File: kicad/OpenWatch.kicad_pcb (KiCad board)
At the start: 2 copper layers, 60 parts, among them J1 USB_microB_2040002-1, J3 Conn_02x05_Odd_Even, J4 Vibration Motor, J6 Conn_01x05, U1 STM32F303RCT6-48, U3 TSP70933DBVR, U7 RT9818A-18GV

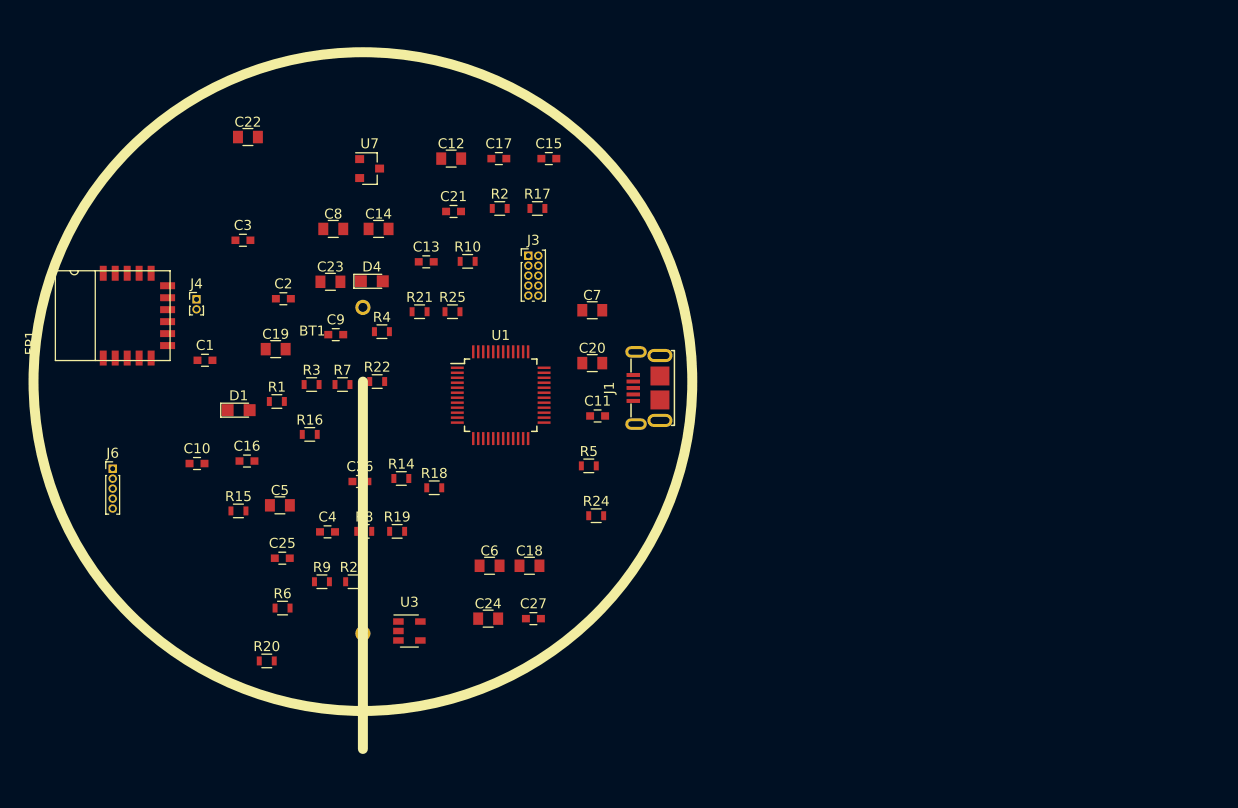
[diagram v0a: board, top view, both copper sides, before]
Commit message: Add all components to be routed to PCB
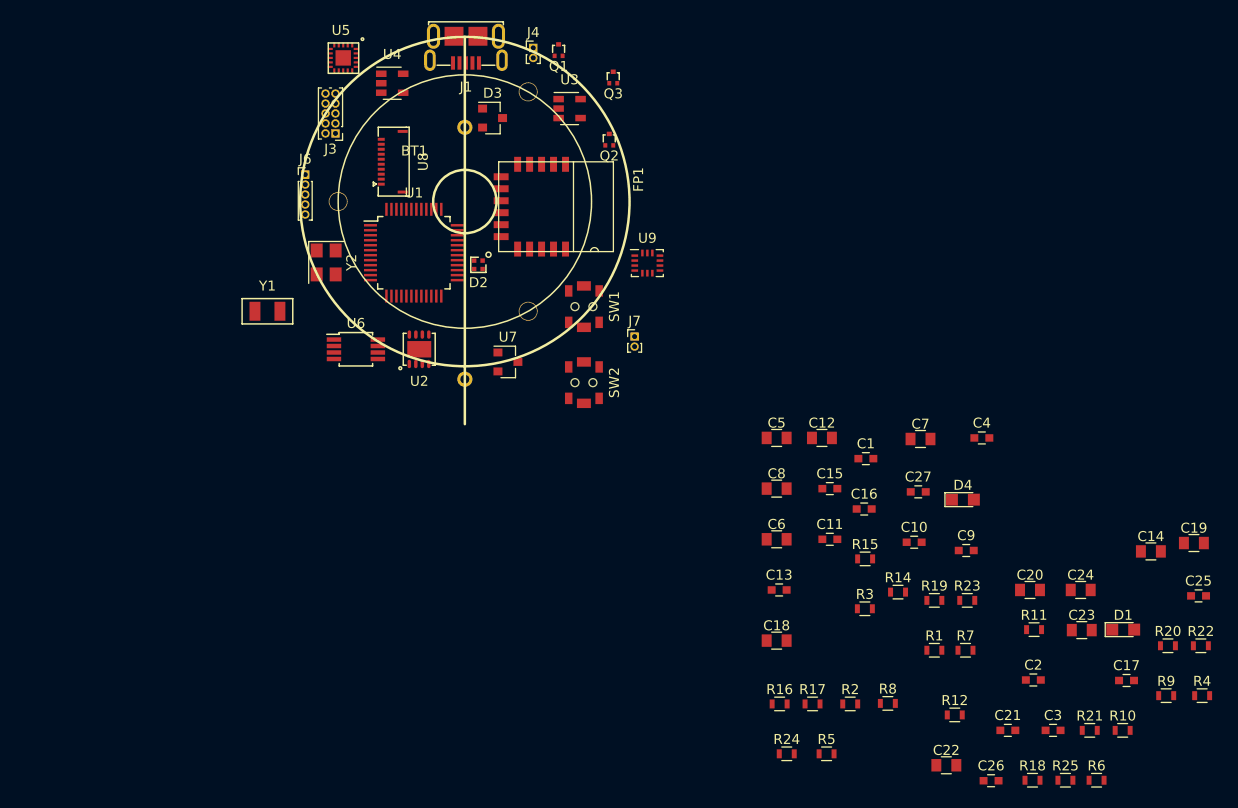
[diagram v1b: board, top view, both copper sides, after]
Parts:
- added D2: LED_ARGB, open_watch:SMLP34RGB2W3, F.Cu at (141.8, 104.6)
- added D3: BAT54, TO_SOT_Packages_SMD:SOT-23, F.Cu at (143.2, 89.8)
- added J7: Conn_01x02, Pin_Headers:Pin_Header_Straight_1x02_Pitch1.00mm, F.Cu at (157.5, 111.8)
- added Q1: RUM002N02T2L, open_watch:VMT3, F.Cu at (149.9, 82.5)
- added Q2: RUM002N02T2L, open_watch:VMT3, F.Cu at (154.9, 91.4)
- added Q3: RUM002N02T2L, open_watch:VMT3, F.Cu at (155.3, 85.2)
- added R11: DNP-0, Resistors_SMD:R_0603, F.Cu at (197.5, 141.1)
- added R12: DNP-0, Resistors_SMD:R_0603, F.Cu at (189.6, 149.7)
- added SW1: SW_Push, open_watch:PTS820_J15M_SMTR_LFS, F.Cu at (152.4, 108.8)
- added SW2: SW_Push, open_watch:PTS820_J15M_SMTR_LFS, F.Cu at (152.4, 116.4)
- added U2: TPS2113ADRBR, open_watch:SON-8, F.Cu at (135.9, 113.0)
- added U4: MCP73831T-2ACI, TO_SOT_Packages_SMD:SOT-23-5, F.Cu at (133.2, 86.4)
- added U5: AT42QT1070-MMHR, open_watch:AT42QT1070-MMHR, F.Cu at (126.8, 82.3)
- added U6: TPS60241DGKR, Housings_SSOP:MSOP-8_3x3mm_Pitch0.65mm, F.Cu at (129.5, 113.0)
- added U8: WM1389CT-ND, open_watch:Molex_FPC_5034801000, F.Cu at (134.9, 94.2)
- added U9: LSM6DSL, Housings_LGA:Bosch_LGA-14_3x2.5mm_Pitch0.5mm, F.Cu at (158.8, 104.4)
- added Y1: ECS.327, open_watch:ECX-31B, F.Cu at (120.7, 109.2)
- added Y2: FA-238, Crystals:Crystal_SMD_SeikoEpson_FA238V-4pin_3.2x2.5mm, F.Cu at (126.6, 104.3)
- moved C3 94.9 mm to (199.4, 151.2)
- moved C22 94.2 mm to (188.7, 154.7)
- moved C19 94.1 mm to (213.6, 132.5)
- moved C25 91.9 mm to (214.0, 137.8)
- moved D1 91.4 mm to (206.5, 141.1)
- moved R20 90.4 mm to (210.9, 142.8)
- moved R4 90.0 mm to (214.4, 147.8)
- moved R22 86.7 mm to (214.2, 142.8)
- moved R9 85.4 mm to (210.8, 147.8)
- moved C2 84.3 mm to (197.5, 146.2)
- moved C14 83.9 mm to (209.2, 133.3)
- moved R6 83.4 mm to (203.8, 156.2)
- moved C23 83.0 mm to (202.3, 141.2)
- moved C17 81.8 mm to (206.8, 146.2)
- moved R10 80.8 mm to (206.4, 151.2)
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
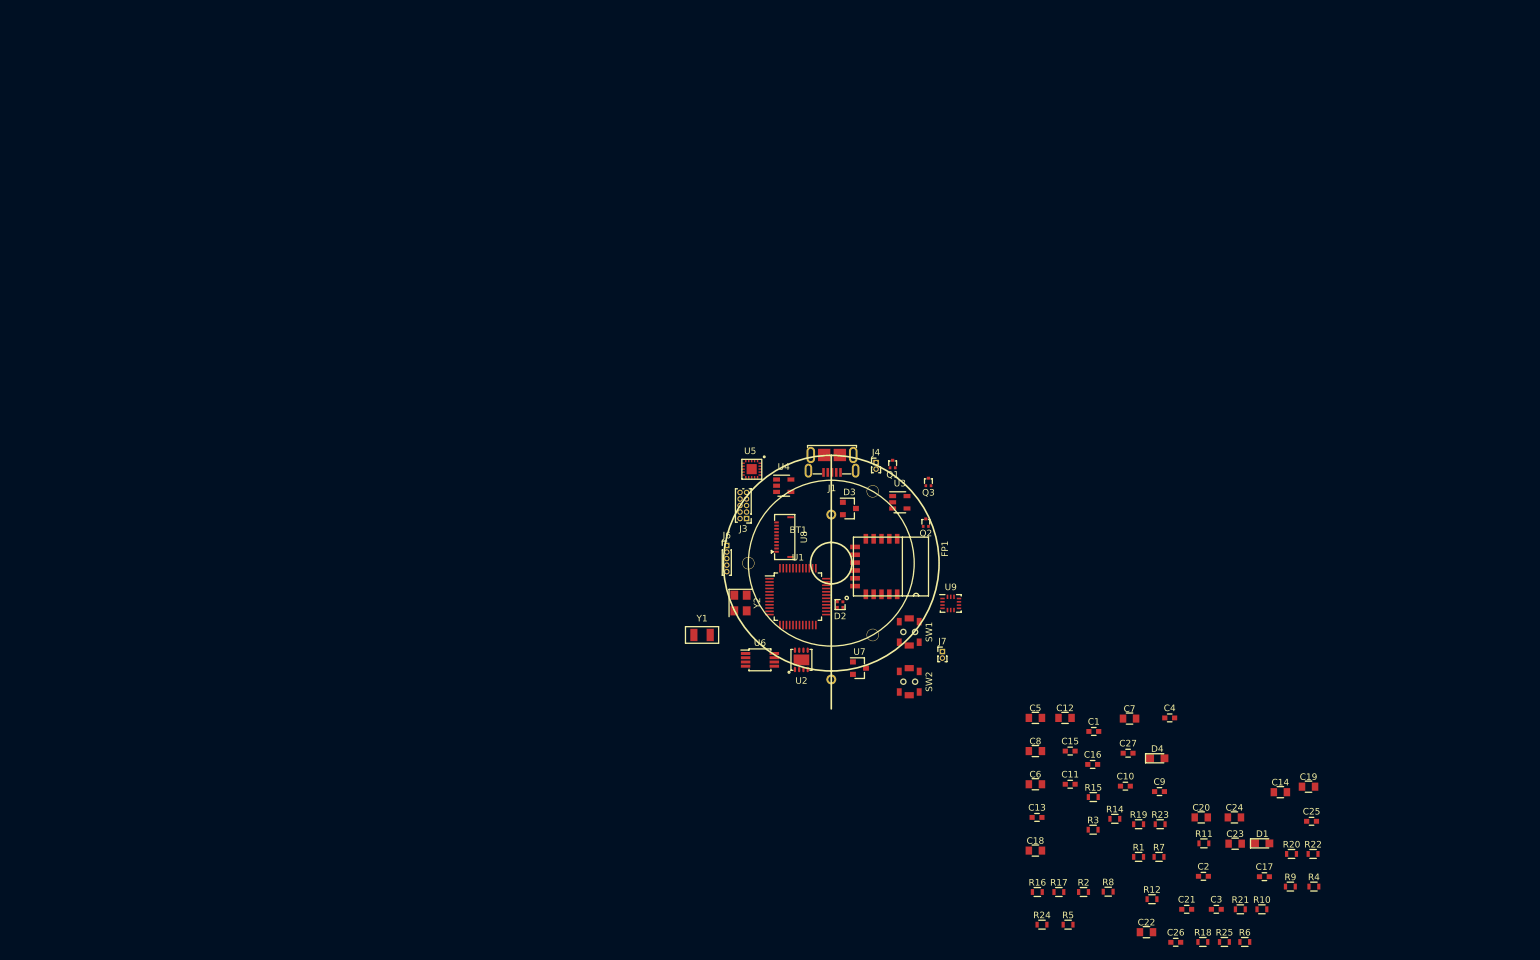
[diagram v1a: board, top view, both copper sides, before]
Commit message: Spread out components
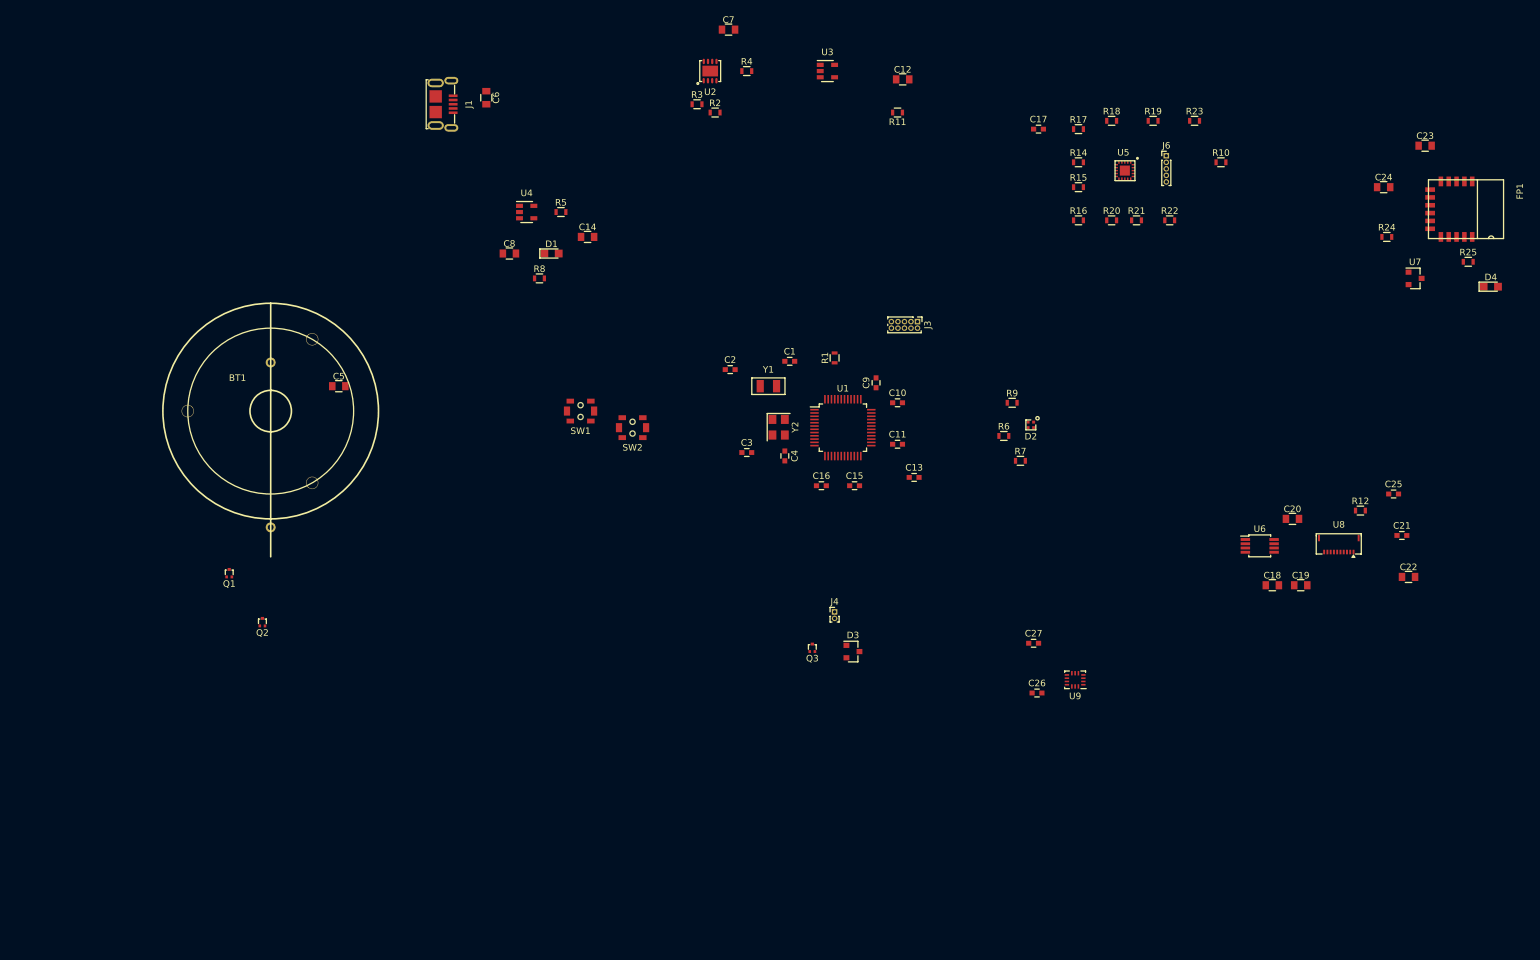
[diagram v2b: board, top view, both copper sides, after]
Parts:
- removed J7: Conn_01x02, Pin_Headers:Pin_Header_Straight_1x02_Pitch1.00mm
- moved R4 152.1 mm to (127.5, 22.9)
- moved D1 141.4 mm to (97.6, 50.8)
- moved C14 136.0 mm to (103.1, 48.3)
- moved C6 134.6 mm to (87.6, 26.9), turned to 270 degrees
- moved R5 133.9 mm to (99.1, 44.5)
- moved R2 132.0 mm to (122.7, 29.2)
- moved R8 128.1 mm to (95.8, 54.6)
- moved R3 126.6 mm to (119.9, 27.9)
- moved R18 126.5 mm to (183.4, 30.5)
- moved C7 122.1 mm to (124.7, 16.5)
- moved R11 121.4 mm to (150.6, 29.2), turned to 180 degrees
- moved C17 119.6 mm to (172.2, 31.8)
- moved C5 118.2 mm to (65.0, 71.1)
- moved R24 117.8 mm to (225.5, 48.3)
- moved R17 116.9 mm to (178.3, 31.8)
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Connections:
- U1 pad 15: /IMU_SCL -> /DISP_SCLK
- U1 pad 17: /IMU_SDI -> /DISP_SDI
- U1 pad 26: /DISP_SCLK -> Net-(U1-Pad26)
- U1 pad 28: /DISP_SDI -> /EXTCOMIN
- U8 pad 4: Net-(J7-Pad2) -> /EXTCOMIN
- U8 pad 8: Net-(J7-Pad1) -> +5V
- U9 pad 13: /IMU_SCL -> /DISP_SCLK
- U9 pad 14: /IMU_SDI -> /DISP_SDI
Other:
- copper layers 2 -> 4

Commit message: Initial placement of critical components
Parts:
- removed R12: DNP-0, Resistors_SMD:R_0603
- C18, C19, C20, C21, C22, C25, C5: moved to B.Cu
- moved C22 176.3 mm to (61.2, 45.7), turned to 180 degrees
- moved C25 171.1 mm to (59.2, 52.1)
- moved C21 170.8 mm to (63.0, 49.5), turned to 180 degrees
- moved C19 168.7 mm to (51.1, 52.1), turned to 180 degrees
- moved U8 167.4 mm to (54.6, 58.2)
- moved U6 166.0 mm to (47.0, 48.3), turned to 270 degrees
- moved C18 165.9 mm to (48.5, 55.9)
- moved C20 150.4 mm to (66.0, 51.8), turned to 90 degrees
- moved J1 48.3 mm to (71.6, 75.5), turned to 90 degrees
- moved C6 40.7 mm to (65.3, 61.0), turned to 180 degrees
- moved R11 26.7 mm to (123.9, 30.5)
- moved C12 26.7 mm to (124.7, 25.4)
- moved C7 26.7 mm to (98.1, 17.8)
- moved R2 26.7 mm to (96.0, 30.5)
- moved R3 26.7 mm to (93.2, 29.2)
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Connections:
- C21 pad 1: Net-(C21-Pad1) -> +5V
- C22 pad 1: Net-(C21-Pad1) -> +5V
- C25 pad 1: Net-(C25-Pad1) -> /DISP_EN
- U1 pad 27: Net-(U1-Pad27) -> /DISP_EN
- U8 pad 5: Net-(C25-Pad1) -> /DISP_EN
- U8 pad 6: Net-(C21-Pad1) -> +5V
- U8 pad 7: Net-(C21-Pad1) -> +5V
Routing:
- net Net-(BT1-Pad2): track 0.00 -> 7.60 mm
- net /VBATT: track 0.00 -> 2.34 mm
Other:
- net class Default: trace_width 0.25 -> 0.2032

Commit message: Second iteration of placement
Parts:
- added R12: 100K, Resistors_SMD:R_0603, F.Cu at (61.5, 58.4)
- added R13: 100K, Resistors_SMD:R_0603, F.Cu at (71.1, 64.8)
- added R26: 100K, Resistors_SMD:R_0603, F.Cu at (126.8, 121.9)
- BT1: footprint open_watch:BH3000 -> Pin_Headers:Pin_Header_Straight_1x02_Pitch2.00mm
- moved D4 220.6 mm to (21.8, 76.2)
- moved R25 216.5 mm to (22.1, 68.6)
- moved C23 210.9 mm to (22.6, 63.5)
- moved U7 210.1 mm to (21.9, 83.8)
- moved C24 205.7 mm to (21.9, 72.4)
- moved R24 205.7 mm to (22.3, 80.0)
- moved FP1 186.8 mm to (51.0, 86.4), turned to 90 degrees
- moved R10 167.1 mm to (33.5, 49.5)
- moved R23 158.5 mm to (39.9, 57.1)
- moved R22 151.4 mm to (41.2, 54.6)
- moved R21 150.1 mm to (37.4, 54.6)
- moved J6 147.8 mm to (44.5, 48.1)
- moved R19 146.7 mm to (43.7, 44.5)
- moved R20 146.2 mm to (37.4, 52.1)
- moved U5 145.2 mm to (39.1, 48.0)
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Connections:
- J1 pad 2: /D+ -> /D_N
- J1 pad 3: /D- -> /D_P
- U1 pad 32: /D- -> /D_N
- U1 pad 33: /D+ -> /D_P
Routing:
- net Net-(BT1-Pad2): track 7.60 -> 0.00 mm
- net /VBATT: track 2.34 -> 0.00 mm

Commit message: Add majority of routing
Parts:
- C1, C12, C14, C2, C23, C24, C3, C4, C6, C7, C8, R11, R14, R15, R16, R17, R18, R2, R24, R25, R3, R4, R5, R6, R7, R8, R9: moved to B.Cu
- moved D3 112.2 mm to (27.6, 96.5)
- moved J4 112.2 mm to (24.8, 90.4)
- moved Q3 112.2 mm to (21.4, 95.4)
- moved R26 112.2 mm to (16.9, 99.1)
- moved D2 97.7 mm to (73.5, 83.0), turned to 90 degrees
- moved R9 96.1 mm to (72.6, 84.3), turned to 270 degrees
- moved R7 95.3 mm to (74.2, 84.3), turned to 270 degrees
- moved R6 93.8 mm to (73.2, 82.3), turned to 180 degrees
- moved C1 82.7 mm to (52.1, 77.5), turned to 270 degrees
- moved Y2 81.4 mm to (51.1, 81.8)
- moved C4 81.3 mm to (52.1, 81.8), turned to 90 degrees
- moved Y1 80.3 mm to (50.8, 77.5)
- moved C3 77.4 mm to (50.2, 81.8), turned to 270 degrees
- moved C12 76.6 mm to (66.4, 74.9)
- moved C2 76.0 mm to (49.5, 77.5), turned to 270 degrees
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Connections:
- U1 pad 13: /LED_RED -> /IMU_CS
- U1 pad 2: /BLE_nRST -> Net-(U1-Pad2)
- U1 pad 20: /IMU_CS -> /DISP_SCS
- U1 pad 25: Net-(U1-Pad25) -> /BLE_nRST
- U1 pad 26: Net-(U1-Pad26) -> /BLE_CONF
- U1 pad 29: /DISP_SCS -> /LED_RED
- U1 pad 40: /BLE_CONF -> Net-(U1-Pad40)
- U1 pad 41: /TOUCH_4 -> /TOUCH_0
- U1 pad 42: /TOUCH_3 -> /TOUCH_4
- U1 pad 43: /TOUCH_2 -> /TOUCH_3
- U1 pad 45: /TOUCH_1 -> /TOUCH_2
- U1 pad 46: /TOUCH_0 -> /TOUCH_1
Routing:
- net GND: track 0.00 -> 35.6 mm, vias 0 -> 8
- net /VUSB: track 0.00 -> 29.5 mm, vias 0 -> 3
- net /VBATT: track 0.00 -> 28.4 mm, vias 0 -> 1
- net /STM_NRST: track 0.00 -> 22.1 mm, vias 0 -> 1
- net /BLE_nRST: track 0.00 -> 21.7 mm, vias 0 -> 3
- net /DISP_SDI: track 0.00 -> 18.6 mm, vias 0 -> 2
- net /DISP_SCLK: track 0.00 -> 17.8 mm
- net /D_N: track 0.00 -> 16.4 mm
- net /D_P: track 0.00 -> 16.4 mm
- net /BLE_CONF: track 0.00 -> 15.9 mm, vias 0 -> 2
- net +3V3: track 0.00 -> 13.3 mm, vias 0 -> 3
- net /TDO: track 0.00 -> 13.1 mm
- net /TDI: track 0.00 -> 12.9 mm, vias 0 -> 1
- net Net-(C7-Pad1): track 0.00 -> 11.2 mm, vias 0 -> 2
- net /IMU_SDO: track 0.00 -> 11.2 mm, vias 0 -> 2
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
